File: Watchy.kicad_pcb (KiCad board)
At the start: 2 copper layers, 33.8 x 46 mm, 57 parts, among them J1 FPC24(0.5MM), J2 Micro USB, J3 Battery, M1 Vibration_Motor, Q1 AO3400A, Q2 UMH3N, Q4 CJ2301, Q5 S8050, SW1 BTN, SW2 BTN, SW3 BTN, SW4 BTN, U1 ESP32-PICO-D4, U2 ME6211C33M5G-N, U3 CP2104, U4 BMA423, U5 TP4054, U6 DS3231MZ

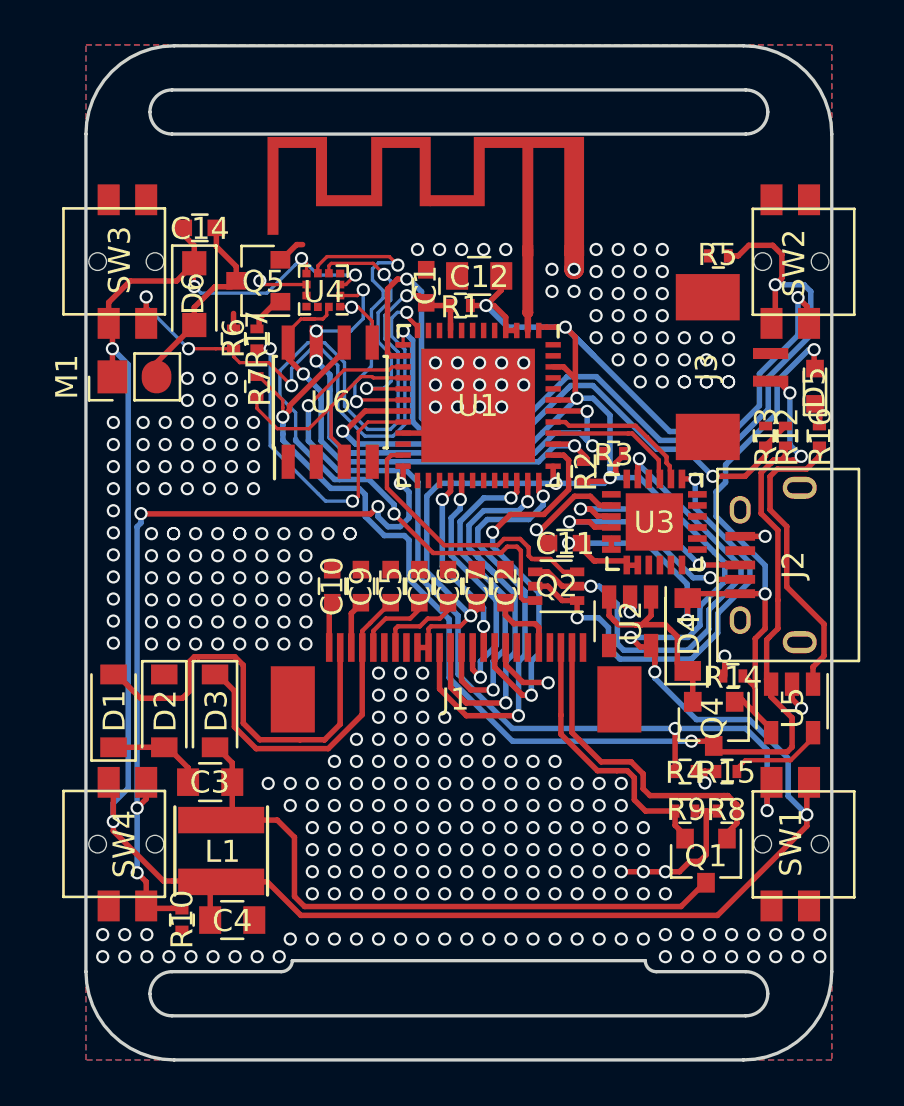
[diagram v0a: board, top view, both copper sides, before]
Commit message: Modifications done during livestream 18th January 2021 for a schmartwatch 2.0 based on the Watchy
- Use DCDC switch mode power supply
- Change RTC to RV-3028
- Use a chip antenna for BLE/WiFi connection
- Review of e-Paper connector for 3 color e-ink
- Forward annotation and initial placing done for PCB
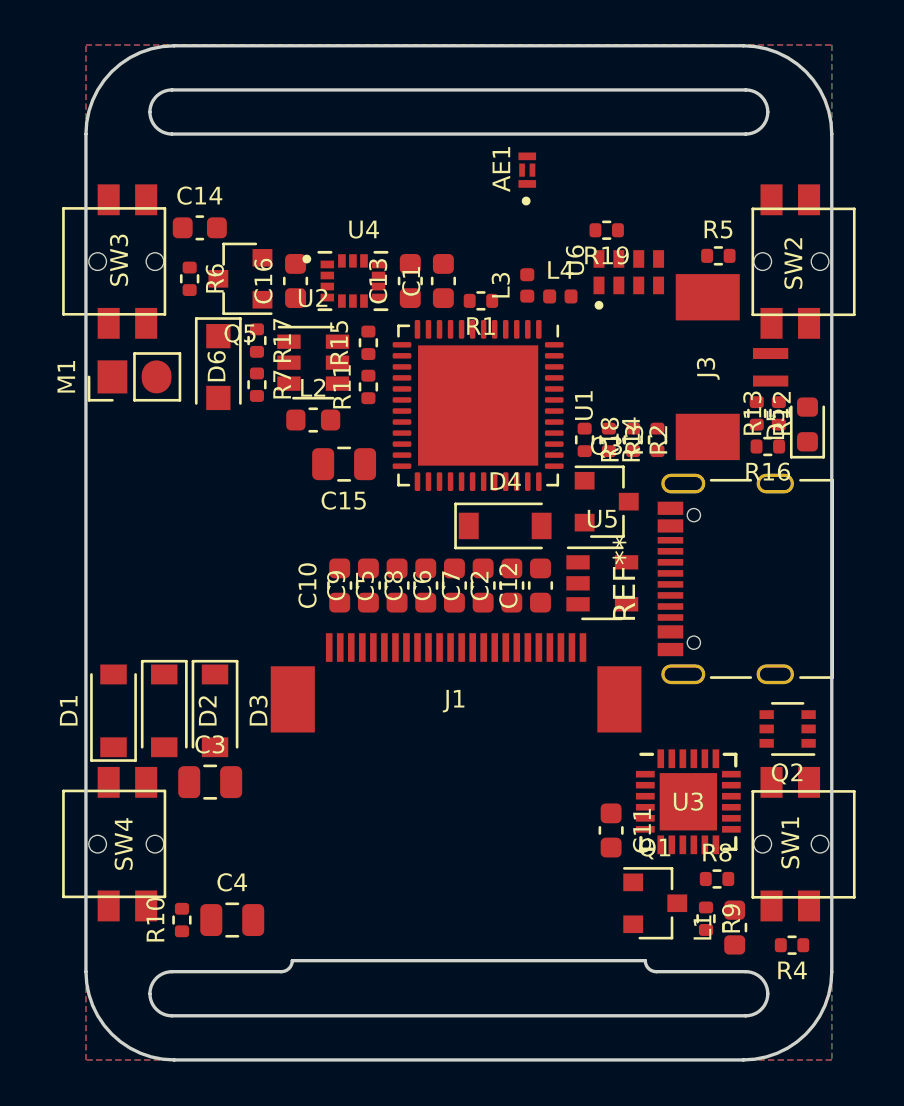
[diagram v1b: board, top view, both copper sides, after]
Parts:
- removed G***: LOGO, Watchy:sqfmi_logo
- removed J2: Micro USB, Watchy:USB_Micro-B
- removed Q4: CJ2301, TO_SOT_Packages_SMD:SOT-23
- removed the REF** at (85.6, 93.2)
- added C13: 100nF, Capacitor_SMD:C_0603_1608Metric, F.Cu at (83.4, 80.8)
- added C15: 4.7uF/50V, Capacitor_SMD:C_0805_2012Metric, F.Cu at (80.4, 89.1)
- added C16: 100nF, Capacitor_SMD:C_0603_1608Metric, F.Cu at (78.2, 80.8)
- added L2: 2u2H, Inductor_SMD:L_0603_1608Metric, F.Cu at (79.0, 87.1)
- added L3: 2nH, Inductor_SMD:L_0402_1005Metric, F.Cu at (88.7, 81.0)
- added L4: 3nH, Inductor_SMD:L_0402_1005Metric, F.Cu at (90.2, 81.5)
- added Q3: CJ2301, Package_TO_SOT_SMD:SOT-23, F.Cu at (92.3, 90.8)
- added R11: 430k, Resistor_SMD:R_0402_1005Metric, F.Cu at (81.5, 85.6)
- added R18: 10K, Resistor_SMD:R_0402_1005Metric, F.Cu at (91.3, 88.0)
- added R19: 10K, Resistor_SMD:R_0402_1005Metric, F.Cu at (92.3, 78.5)
- added REF**: USB_C_Receptacle_Palconn_UTC16-G, Connector_USB:USB_C_Receptacle_Palconn_UTC16-G, F.Cu at (97.7, 94.3)
- AE1: value SWRA117D -> Antenna_Chip; footprint Watchy:SWRA117D -> Watchy:ANT_ANT016008LCS2442MA2
- C1, C10, C11, C14, C2, C5, C6, C7, C8, C9: footprint Capacitors_SMD:C_0603 -> Capacitor_SMD:C_0603_1608Metric
- C12: value 4.7uF/50V -> 1uF/50V; footprint Capacitors_SMD:C_0805 -> Capacitor_SMD:C_0603_1608Metric
- C3, C4: footprint Capacitors_SMD:C_0805 -> Capacitor_SMD:C_0805_2012Metric
- D1, D2, D3, D4: footprint Diodes_SMD:D_SOD-123 -> Diode_SMD:D_SOD-123
- D5: footprint LEDs:LED_0603 -> LED_SMD:LED_0603_1608Metric
- L1: value 10uH 1A -> 2u2H; footprint Inductors:Inductor_Taiyo-Yuden_NR-40xx -> Inductor_SMD:L_0603_1608Metric
- Q1, Q5: footprint TO_SOT_Packages_SMD:SOT-23 -> Package_TO_SOT_SMD:SOT-23
- Q2: footprint TO_SOT_Packages_SMD:SOT-363_SC-70-6 -> Package_TO_SOT_SMD:SOT-363_SC-70-6
- R1, R10, R12, R13, R14, R16, R17, R2, R3, R4, R5, R6, R7, R8, R9: footprint Resistors_SMD:R_0402 -> Resistor_SMD:R_0402_1005Metric
- R15: value 10K -> 100K; footprint Resistors_SMD:R_0402 -> Resistor_SMD:R_0402_1005Metric
- U1: footprint Housings_DFN_QFN:QFN-48-1EP_7x7mm_Pitch0.5mm -> Package_DFN_QFN:QFN-48-1EP_7x7mm_P0.5mm_EP5.45x5.45mm
- U2: value ME6211C33M5G-N -> MT3420C; footprint TO_SOT_Packages_SMD:SOT-23-5 -> Package_TO_SOT_SMD:SOT-23-6
- U4: value BMA423 -> LSM6DSOXTR; footprint Housings_LGA:LGA-12_2x2mm_Pitch0.5mm -> Watchy:PQFN50P250X300X86-14N
- U5: footprint TO_SOT_Packages_SMD:SOT-23-5 -> Package_TO_SOT_SMD:SOT-23-5
- U6: value DS3231MZ -> RV-3028-C7; footprint Housings_SOIC:SOIC-8_3.9x4.9mm_Pitch1.27mm -> Watchy:IC_RV-3028-C7
- moved R15 25.3 mm to (81.5, 83.6), turned to 90 degrees
- moved L1 23.5 mm to (98.1, 110.1), turned to 90 degrees
- moved U2 18.5 mm to (79.0, 84.5), turned to 0 degrees
- moved AE1 14.8 mm to (88.7, 75.8), turned to 90 degrees
- moved U6 14.8 mm to (93.3, 80.4)
- moved C12 14.3 mm to (89.3, 94.6), turned to 90 degrees
- moved C11 13.2 mm to (92.5, 105.7), turned to 270 degrees
- moved U3 12.8 mm to (96.0, 104.4)
- moved Q2 12.3 mm to (100.5, 101.1)
- moved R14 11.2 mm to (94.6, 88.0), turned to 90 degrees
- moved U5 10.3 mm to (92.1, 94.5), turned to 0 degrees
- moved D4 9.62 mm to (87.7, 91.9), turned to 0 degrees
- moved R4 9.24 mm to (100.7, 110.9)
- moved R9 4.97 mm to (96.8, 109.7), turned to 270 degrees
- moved D6 3.48 mm to (74.7, 84.7)
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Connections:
- AE1 pad 1: Net-(AE1-Pad1) -> (no net)
- AE1 pad 2: GND -> (no net)
- C12 pad 1: +3V3 -> Net-(C12-Pad1)
- J1 pad 1: Net-(J1-Pad1) -> (no net)
- J1 pad 19: Net-(J1-Pad19) -> (no net)
- J1 pad 4: Net-(J1-Pad4) -> Net-(C12-Pad1)
- J1 pad 6: Net-(J1-Pad6) -> (no net)
- J1 pad 7: Net-(J1-Pad7) -> (no net)
- R15 pad 1: GND -> Net-(R11-Pad2)
- R15 pad 2: Net-(R15-Pad2) -> GND
- R7 pad 1: +BATT -> +3V3
- U1 pad 10: Net-(U1-Pad10) -> (no net)
- U1 pad 11: Net-(U1-Pad11) -> (no net)
- U1 pad 2: Net-(AE1-Pad1) -> Net-(L3-Pad1)
- U1 pad 22: Net-(U1-Pad22) -> (no net)
- U1 pad 25: Net-(U1-Pad25) -> (no net)
- U1 pad 26: Net-(U1-Pad26) -> (no net)
- U1 pad 27: Net-(U1-Pad27) -> (no net)
- U1 pad 30: Net-(U1-Pad30) -> (no net)
- U1 pad 31: Net-(U1-Pad31) -> (no net)
- U1 pad 32: Net-(U1-Pad32) -> (no net)
- U1 pad 33: Net-(U1-Pad33) -> (no net)
- U1 pad 44: Net-(U1-Pad44) -> (no net)
- U1 pad 45: Net-(U1-Pad45) -> (no net)
- U1 pad 47: Net-(U1-Pad47) -> (no net)
- U1 pad 48: Net-(U1-Pad48) -> (no net)
- U1 pad 5: Net-(U1-Pad5) -> (no net)
- U1 pad 6: Net-(U1-Pad6) -> (no net)
- U1 pad 7: Net-(U1-Pad7) -> (no net)
- U1 pad 8: Net-(U1-Pad8) -> (no net)
- U2 pad 3: Net-(D4-Pad1) -> Net-(L2-Pad1)
- U2 pad 4: Net-(U2-Pad4) -> Net-(D4-Pad1)
- U2 pad 5: +3V3 -> (no net)
- U3 pad 1: Net-(U3-Pad1) -> (no net)
- U3 pad 10: Net-(U3-Pad10) -> (no net)
- U3 pad 11: Net-(U3-Pad11) -> (no net)
- U3 pad 12: Net-(U3-Pad12) -> (no net)
- U3 pad 13: Net-(U3-Pad13) -> (no net)
- U3 pad 14: Net-(U3-Pad14) -> (no net)
- U3 pad 15: Net-(U3-Pad15) -> (no net)
- U3 pad 16: Net-(U3-Pad16) -> (no net)
- U3 pad 17: Net-(U3-Pad17) -> (no net)
- U3 pad 18: Net-(U3-Pad18) -> (no net)
- U3 pad 22: Net-(U3-Pad22) -> (no net)
- U3 pad 24: Net-(U3-Pad24) -> (no net)
- U3 pad 5: Net-(U3-Pad5) -> (no net)
- U3 pad 6: Net-(U3-Pad5) -> (no net)
- U3 pad 9: Net-(U3-Pad9) -> (no net)
- U4 pad 10: Net-(U4-Pad10) -> (no net)
- U4 pad 11: Net-(U4-Pad11) -> (no net)
- U4 pad 12: SCL -> +3V3
- U4 pad 2: SDA -> GND
- U4 pad 3: +3V3 -> GND
- U4 pad 4: Net-(U4-Pad4) -> ACC_INT_1
- U4 pad 5: ACC_INT_1 -> +3V3
- U4 pad 6: ACC_INT_2 -> GND
- U4 pad 7: +3V3 -> GND
- U4 pad 8: GND -> +3V3
- U4 pad 9: GND -> ACC_INT_2
- U5 pad 5: Net-(R15-Pad2) -> Net-(R18-Pad2)
- U6 pad 1: Net-(U6-Pad1) -> (no net)
- U6 pad 2: GND -> RTC_INT
- U6 pad 3: RTC_INT -> SCL
- U6 pad 4: Net-(U6-Pad4) -> SDA
- U6 pad 7: SDA -> +3V3
- U6 pad 8: SCL -> Net-(R19-Pad2)
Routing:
- net +3V3: track 187.0 -> 0.00 mm, vias 16 -> 0
- net +BATT: track 62.5 -> 0.00 mm, vias 4 -> 0
- net BTN_1: track 43.3 -> 0.00 mm, vias 3 -> 0
- net BTN_2: track 43.2 -> 0.00 mm, vias 2 -> 0
- net VBUS: track 39.3 -> 0.00 mm, vias 4 -> 0
- net EN: track 38.0 -> 0.00 mm, vias 2 -> 0
- net BTN_4: track 36.8 -> 0.00 mm, vias 5 -> 0
- net GND: track 31.9 -> 0.00 mm, vias 333 -> 0
- net Net-(C3-Pad2): track 29.1 -> 0.00 mm
- net SDA: track 27.9 -> 0.00 mm, vias 5 -> 0
- net ADC: track 26.0 -> 0.00 mm, vias 2 -> 0
- net BTN_3: track 26.0 -> 0.00 mm, vias 4 -> 0
- net SCL: track 22.9 -> 0.00 mm, vias 2 -> 0
- net DTR: track 21.7 -> 0.00 mm, vias 2 -> 0
- net MOSI: track 20.5 -> 0.00 mm, vias 2 -> 0
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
